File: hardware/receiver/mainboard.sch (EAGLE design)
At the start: 5 parts, among them U1 ATMEGA328P_TQFP, U2 RFM69HCW

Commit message: Preliminary schematic
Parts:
- added C1: 10u, SparkFun-Passives:CAP1206
- added C2, C3: 100n, SparkFun-Passives:CAP0603-CAP
- added J3: AVR_SPI_PRG_6PTH, SparkFun-Connectors:AVR_SPI_PRG_6PTH
- added J4: (no value), SparkFun-Connectors:M02PTH
- added Q1: MOSFET-NCHANNELAO3404A, SparkFun-DiscreteSemi:MOSFET-NCHANNELAO3404A
- added R1: (no value), SparkFun-Passives:RESISTOR0603-RES
- added R2: 10k, SparkFun-Passives:RESISTOR0603-RES
- J2: value (none) -> POWER_JACKPTH; device SparkFun-Connectors:M025MM -> SparkFun-Connectors:POWER_JACKPTH
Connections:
- new net GND: C1.2, C2.2, C3.2, J2.GND, J2.GNDBREAK, J3.6, J4.2, Q1.S, R2.1, U1.AGND, U1.GND@3, U1.GND@5, U2.GND@1, U2.GND@2
- new net MISO: J3.1, U2.MOSI
- new net MOSI: J3.4, U2.MISO
- new net N$1: U1.PD4(XCK/T0), U2.NSS
- new net N$2: J3.5, R1.2, U1.PC6(/RESET)
- new net N$3: U1.PD3(INT1), U2.DIO0
- new net N$4: J4.1, U2.ANT
- new net N$5: J1.1, U$1.MAIN
- new net N$6: J1.2, U$1.NO
- new net N$7: Q1.D, U$1.COIL2
- new net N$8: Q1.G, R2.2, U1.PD5(T1)
- new net SCK: J3.3, U2.SCK
- new net VCC: C1.1, C2.1, C3.1, J2.PWR, J3.2, R1.1, U$1.COIL1, U1.AVCC, U1.VCC@4, U1.VCC@6, U2.3.3V
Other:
- moved on the sheet: J1, J2, U$1, U1

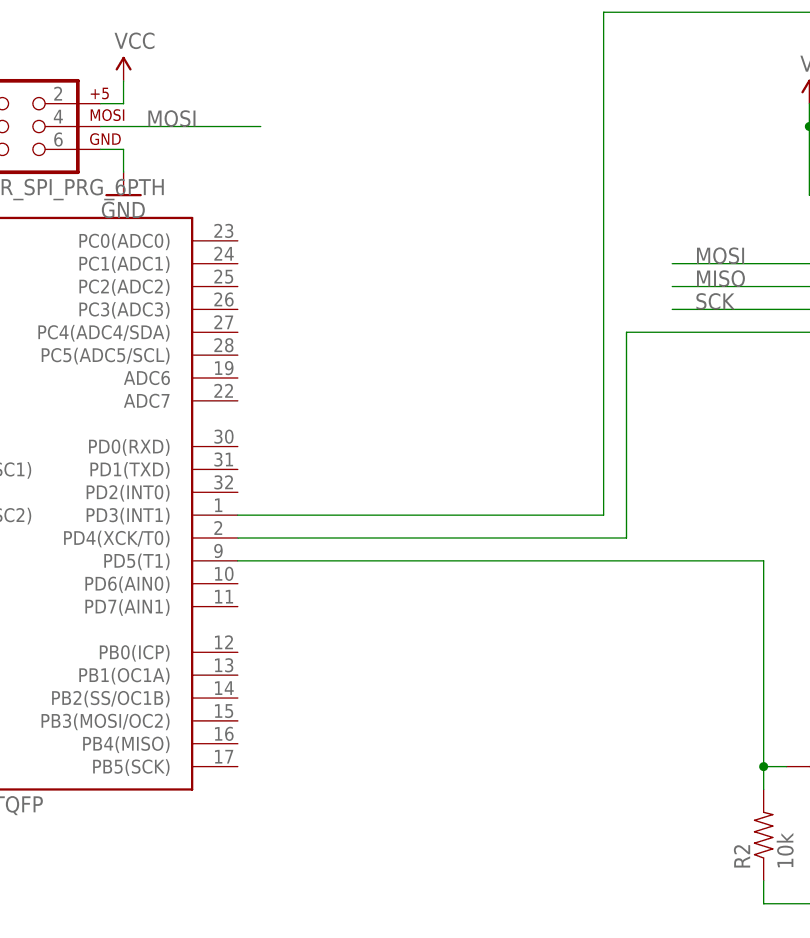
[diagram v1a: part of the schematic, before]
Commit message: Added expansion connector
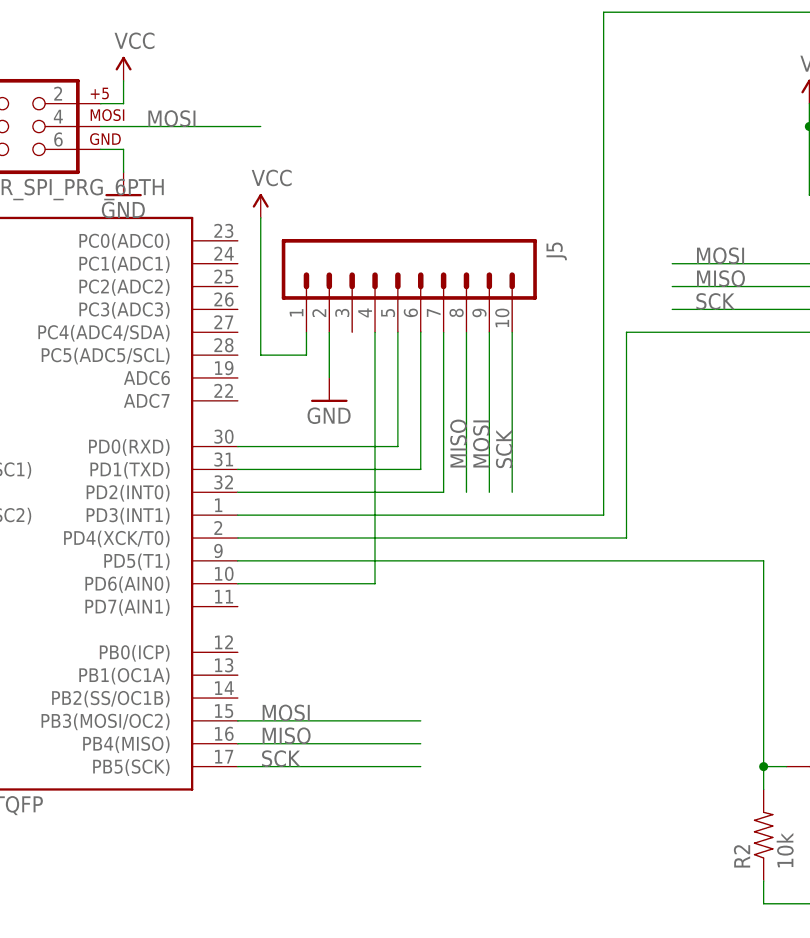
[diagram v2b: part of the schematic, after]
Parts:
- added J5: (no value), SparkFun-Connectors:M10SILK_FEMALE_PTH
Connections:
- new net N$10: J5.6, U1.PD1(TXD)
- new net N$11: J5.5, U1.PD0(RXD)
- new net N$12: J5.4, U1.PD6(AIN0)
- new net N$9: J5.7, U1.PD2(INT0)
- net GND: now also J5.2
- net MISO: now also J5.8, U1.PB4(MISO)
- net MOSI: now also J5.9, U1.PB3(MOSI/OC2)
- net SCK: now also J5.10, U1.PB5(SCK)
- net VCC: now also J5.1
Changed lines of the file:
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@@
 <part name="GND5" library="SparkFun-Aesthetics" deviceset="GND" device=""/>
 <part name="R2" library="SparkFun-Passives" deviceset="RESISTOR" device="0603-RES" value="10k"/>
+<part name="J5" library="SparkFun-Connectors" deviceset="M10" device="SILK_FEMALE_PTH"/>
+<part name="SUPPLY6" library="SparkFun-Aesthetics" deviceset="VCC" device=""/>
+<part name="GND6" library="SparkFun-Aesthetics" deviceset="GND" device=""/>
 </parts>
 <sheets>
@@
 <instance part="GND5" gate="1" x="167.64" y="-27.94"/>
 <instance part="R2" gate="G$1" x="157.48" y="-15.24" rot="R90"/>
+<instance part="J5" gate="G$1" x="124.46" y="50.8" rot="R270"/>
+<instance part="SUPPLY6" gate="G$1" x="101.6" y="53.34"/>
+<instance part="GND6" gate="1" x="109.22" y="33.02"/>
 </instances>
 <busses>
@@
 <wire x1="157.48" y1="-22.86" x2="167.64" y2="-22.86" width="0.1524" layer="91"/>
 <junction x="167.64" y="-22.86"/>
+</segment>
+<segment>
+<pinref part="GND6" gate="1" pin="GND"/>
+<pinref part="J5" gate="G$1" pin="2"/>
+<wire x1="109.22" y1="35.56" x2="109.22" y2="40.64" width="0.1524" layer="91"/>
 </segment>
 </net>
@@
 <wire x1="167.64" y1="12.7" x2="170.18" y2="12.7" width="0.1524" layer="91"/>
 </segment>
+<segment>
+<pinref part="SUPPLY6" gate="G$1" pin="VCC"/>
+<wire x1="101.6" y1="53.34" x2="101.6" y2="38.1" width="0.1524" layer="91"/>
+<pinref part="J5" gate="G$1" pin="1"/>
+<wire x1="101.6" y1="38.1" x2="106.68" y2="38.1" width="0.1524" layer="91"/>
+<wire x1="106.68" y1="38.1" x2="106.68" y2="40.64" width="0.1524" layer="91"/>
+</segment>
 </net>
 <net name="N$2" class="0">
@@
 <label x="149.86" y="48.26" size="1.778" layer="95"/>
 </segment>
+<segment>
+<pinref part="U1" gate="U$1" pin="PB3(MOSI/OC2)"/>
+<wire x1="99.06" y1="-2.54" x2="119.38" y2="-2.54" width="0.1524" layer="91"/>
+<label x="101.6" y="-2.54" size="1.778" layer="95"/>
+</segment>
+<segment>
+<pinref part="J5" gate="G$1" pin="9"/>
+<wire x1="127" y1="40.64" x2="127" y2="22.86" width="0.1524" layer="91"/>
+<label x="127" y="25.4" size="1.778" layer="95" rot="R90"/>
+</segment>
 </net>
 <net name="SCK" class="0">
@@
 <label x="149.86" y="43.18" size="1.778" layer="95"/>
 </segment>
+<segment>
+<pinref part="U1" gate="U$1" pin="PB5(SCK)"/>
+<wire x1="99.06" y1="-7.62" x2="119.38" y2="-7.62" width="0.1524" layer="91"/>
+<label x="101.6" y="-7.62" size="1.778" layer="95"/>
+</segment>
+<segment>
+<pinref part="J5" gate="G$1" pin="10"/>
+<wire x1="129.54" y1="40.64" x2="129.54" y2="22.86" width="0.1524" layer="91"/>
+<label x="129.54" y="25.4" size="1.778" layer="95" rot="R90"/>
+</segment>
 </net>
 <net name="MISO" class="0">
@@
 <wire x1="165.1" y1="45.72" x2="147.32" y2="45.72" width="0.1524" layer="91"/>
 <label x="149.86" y="45.72" size="1.778" layer="95"/>
+</segment>
+<segment>
+<pinref part="U1" gate="U$1" pin="PB4(MISO)"/>
+<wire x1="99.06" y1="-5.08" x2="119.38" y2="-5.08" width="0.1524" layer="91"/>
+<label x="101.6" y="-5.08" size="1.778" layer="95"/>
+</segment>
+<segment>
+<pinref part="J5" gate="G$1" pin="8"/>
+<wire x1="124.46" y1="40.64" x2="124.46" y2="22.86" width="0.1524" layer="91"/>
+<label x="124.46" y="25.4" size="1.778" layer="95" rot="R90"/>
 </segment>
 </net>
@@
 </segment>
 </net>
+<net name="N$9" class="0">
+<segment>
+<pinref part="J5" gate="G$1" pin="7"/>
+<wire x1="121.92" y1="40.64" x2="121.92" y2="22.86" width="0.1524" layer="91"/>
+<pinref part="U1" gate="U$1" pin="PD2(INT0)"/>
+<wire x1="121.92" y1="22.86" x2="99.06" y2="22.86" width="0.1524" layer="91"/>
+</segment>
+</net>
+<net name="N$10" class="0">
+<segment>
+<pinref part="J5" gate="G$1" pin="6"/>
+<wire x1="119.38" y1="40.64" x2="119.38" y2="25.4" width="0.1524" layer="91"/>
+<pinref part="U1" gate="U$1" pin="PD1(TXD)"/>
+<wire x1="119.38" y1="25.4" x2="99.06" y2="25.4" width="0.1524" layer="91"/>
+</segment>
+</net>
+<net name="N$11" class="0">
+<segment>
+<pinref part="J5" gate="G$1" pin="5"/>
+<wire x1="116.84" y1="40.64" x2="116.84" y2="27.94" width="0.1524" layer="91"/>
+<pinref part="U1" gate="U$1" pin="PD0(RXD)"/>
+<wire x1="116.84" y1="27.94" x2="99.06" y2="27.94" width="0.1524" layer="91"/>
+</segment>
+</net>
+<net name="N$12" class="0">
+<segment>
+<pinref part="J5" gate="G$1" pin="4"/>
+<wire x1="114.3" y1="40.64" x2="114.3" y2="12.7" width="0.1524" layer="91"/>
+<pinref part="U1" gate="U$1" pin="PD6(AIN0)"/>
+<wire x1="114.3" y1="12.7" x2="99.06" y2="12.7" width="0.1524" layer="91"/>
+</segment>
+</net>

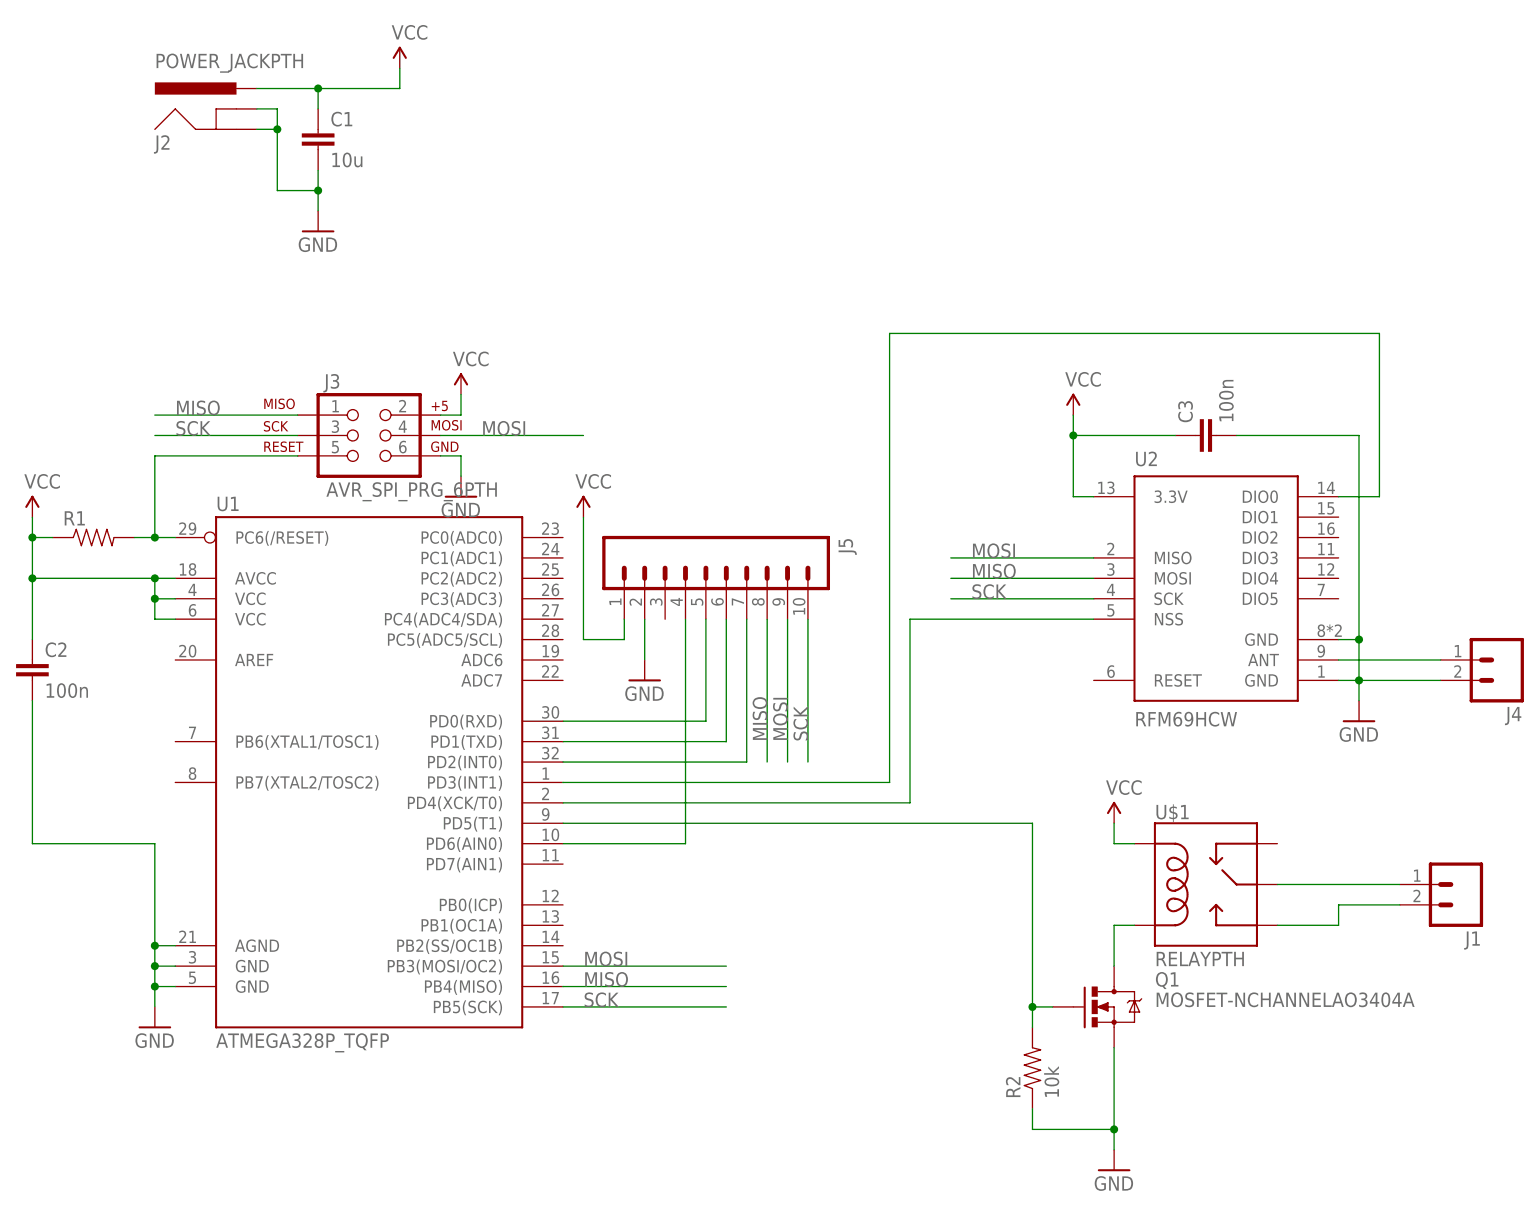
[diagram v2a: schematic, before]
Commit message: Initial PCB layout
* Optimized expansion connector for PCB layout
* Added protection diode to relay
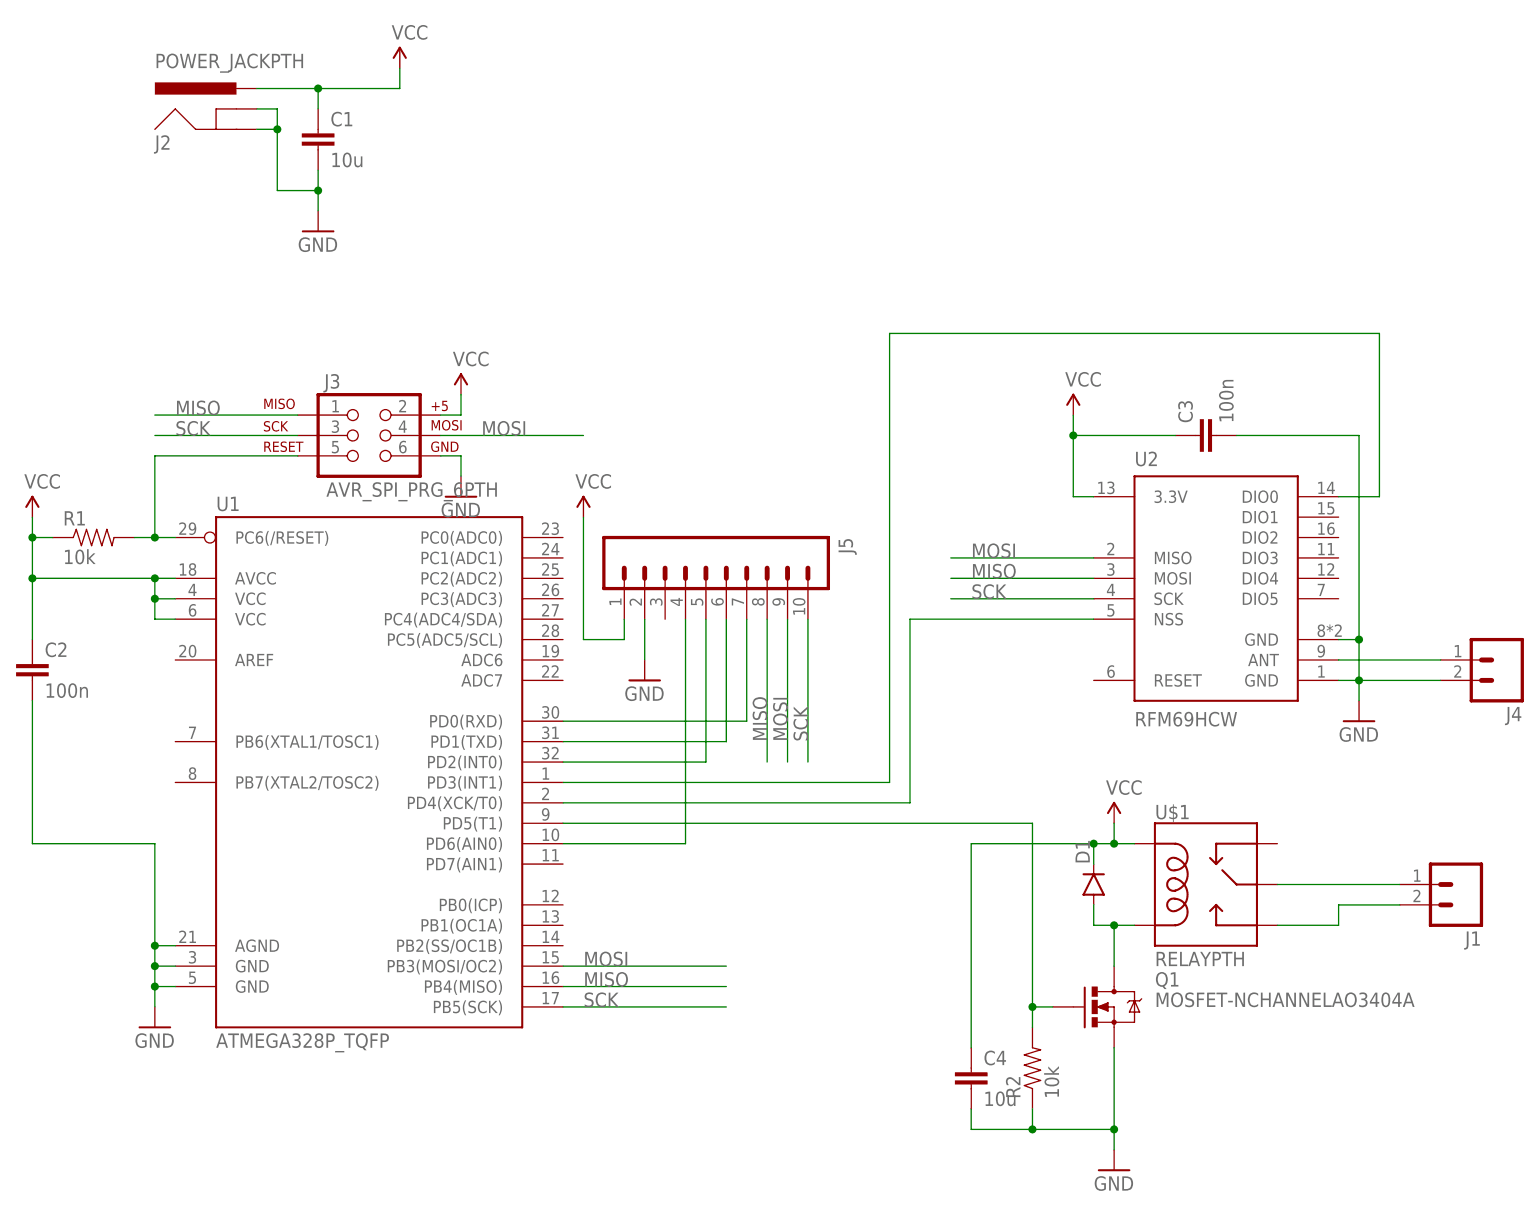
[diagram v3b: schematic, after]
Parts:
- added C4: 10u, SparkFun-Passives:CAP1206
- added D1: (no value), SparkFun-DiscreteSemi:DIODEBAS16
- R1: value (none) -> 10k
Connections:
- net GND: now also C4.2
- net N$11: now also U1.PD2(INT0); no longer U1.PD0(RXD)
- net N$7: now also D1.A
- net N$9: now also U1.PD0(RXD); no longer U1.PD2(INT0)
- net VCC: now also C4.1, D1.C
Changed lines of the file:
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@@
 <part name="GND1" library="SparkFun-Aesthetics" deviceset="GND" device=""/>
 <part name="SUPPLY1" library="SparkFun-Aesthetics" deviceset="VCC" device=""/>
-<part name="R1" library="SparkFun-Passives" deviceset="RESISTOR" device="0603-RES"/>
+<part name="R1" library="SparkFun-Passives" deviceset="RESISTOR" device="0603-RES" value="10k"/>
 <part name="SUPPLY2" library="SparkFun-Aesthetics" deviceset="VCC" device=""/>
 <part name="GND2" library="SparkFun-Aesthetics" deviceset="GND" device=""/>
@@
 <part name="SUPPLY6" library="SparkFun-Aesthetics" deviceset="VCC" device=""/>
 <part name="GND6" library="SparkFun-Aesthetics" deviceset="GND" device=""/>
+<part name="D1" library="SparkFun-DiscreteSemi" deviceset="DIODE" device="BAS16"/>
+<part name="C4" library="SparkFun-Passives" deviceset="CAP" device="1206" value="10u"/>
 </parts>
 <sheets>
@@
 <instance part="SUPPLY6" gate="G$1" x="101.6" y="53.34"/>
 <instance part="GND6" gate="1" x="109.22" y="33.02"/>
+<instance part="D1" gate="G$1" x="165.1" y="7.62" rot="R90"/>
+<instance part="C4" gate="G$1" x="149.86" y="-17.78"/>
 </instances>
 <busses>
@@
 <wire x1="157.48" y1="-22.86" x2="167.64" y2="-22.86" width="0.1524" layer="91"/>
 <junction x="167.64" y="-22.86"/>
+<pinref part="C4" gate="G$1" pin="2"/>
+<wire x1="149.86" y1="-20.32" x2="149.86" y2="-22.86" width="0.1524" layer="91"/>
+<wire x1="149.86" y1="-22.86" x2="157.48" y2="-22.86" width="0.1524" layer="91"/>
+<junction x="157.48" y="-22.86"/>
 </segment>
 <segment>
@@
 <pinref part="U$1" gate="K$1" pin="COIL1"/>
 <wire x1="167.64" y1="12.7" x2="170.18" y2="12.7" width="0.1524" layer="91"/>
+<pinref part="D1" gate="G$1" pin="C"/>
+<wire x1="165.1" y1="10.16" x2="165.1" y2="12.7" width="0.1524" layer="91"/>
+<wire x1="165.1" y1="12.7" x2="167.64" y2="12.7" width="0.1524" layer="91"/>
+<junction x="167.64" y="12.7"/>
+<pinref part="C4" gate="G$1" pin="1"/>
+<wire x1="149.86" y1="-12.7" x2="149.86" y2="12.7" width="0.1524" layer="91"/>
+<wire x1="149.86" y1="12.7" x2="165.1" y2="12.7" width="0.1524" layer="91"/>
+<junction x="165.1" y="12.7"/>
 </segment>
 <segment>
@@
 <pinref part="U$1" gate="K$1" pin="COIL2"/>
 <wire x1="167.64" y1="2.54" x2="170.18" y2="2.54" width="0.1524" layer="91"/>
+<pinref part="D1" gate="G$1" pin="A"/>
+<wire x1="165.1" y1="5.08" x2="165.1" y2="2.54" width="0.1524" layer="91"/>
+<wire x1="165.1" y1="2.54" x2="167.64" y2="2.54" width="0.1524" layer="91"/>
+<junction x="167.64" y="2.54"/>
 </segment>
 </net>
@@
 </segment>
 </net>
-<net name="N$9" class="0">
-<segment>
-<pinref part="J5" gate="G$1" pin="7"/>
-<wire x1="121.92" y1="40.64" x2="121.92" y2="22.86" width="0.1524" layer="91"/>
-<pinref part="U1" gate="U$1" pin="PD2(INT0)"/>
-<wire x1="121.92" y1="22.86" x2="99.06" y2="22.86" width="0.1524" layer="91"/>
-</segment>
-</net>
-<net name="N$10" class="0">
-<segment>
-<pinref part="J5" gate="G$1" pin="6"/>
-<wire x1="119.38" y1="40.64" x2="119.38" y2="25.4" width="0.1524" layer="91"/>
-<pinref part="U1" gate="U$1" pin="PD1(TXD)"/>
-<wire x1="119.38" y1="25.4" x2="99.06" y2="25.4" width="0.1524" layer="91"/>
-</segment>
-</net>
-<net name="N$11" class="0">
-<segment>
-<pinref part="J5" gate="G$1" pin="5"/>
-<wire x1="116.84" y1="40.64" x2="116.84" y2="27.94" width="0.1524" layer="91"/>
-<pinref part="U1" gate="U$1" pin="PD0(RXD)"/>
-<wire x1="116.84" y1="27.94" x2="99.06" y2="27.94" width="0.1524" layer="91"/>
-</segment>
-</net>
 <net name="N$12" class="0">
 <segment>
@@
 </segment>
 </net>
+<net name="N$9" class="0">
+<segment>
+<pinref part="J5" gate="G$1" pin="7"/>
+<wire x1="121.92" y1="40.64" x2="121.92" y2="27.94" width="0.1524" layer="91"/>
+<pinref part="U1" gate="U$1" pin="PD0(RXD)"/>
+<wire x1="121.92" y1="27.94" x2="99.06" y2="27.94" width="0.1524" layer="91"/>
+</segment>
+</net>
+<net name="N$10" class="0">
+<segment>
+<pinref part="U1" gate="U$1" pin="PD1(TXD)"/>
+<pinref part="J5" gate="G$1" pin="6"/>
+<wire x1="99.06" y1="25.4" x2="119.38" y2="25.4" width="0.1524" layer="91"/>
+<wire x1="119.38" y1="25.4" x2="119.38" y2="40.64" width="0.1524" layer="91"/>
+</segment>
+</net>
+<net name="N$11" class="0">
+<segment>
+<pinref part="U1" gate="U$1" pin="PD2(INT0)"/>
+<pinref part="J5" gate="G$1" pin="5"/>
+<wire x1="99.06" y1="22.86" x2="116.84" y2="22.86" width="0.1524" layer="91"/>
+<wire x1="116.84" y1="22.86" x2="116.84" y2="40.64" width="0.1524" layer="91"/>
+</segment>
+</net>
